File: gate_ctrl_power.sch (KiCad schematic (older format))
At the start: 1 part

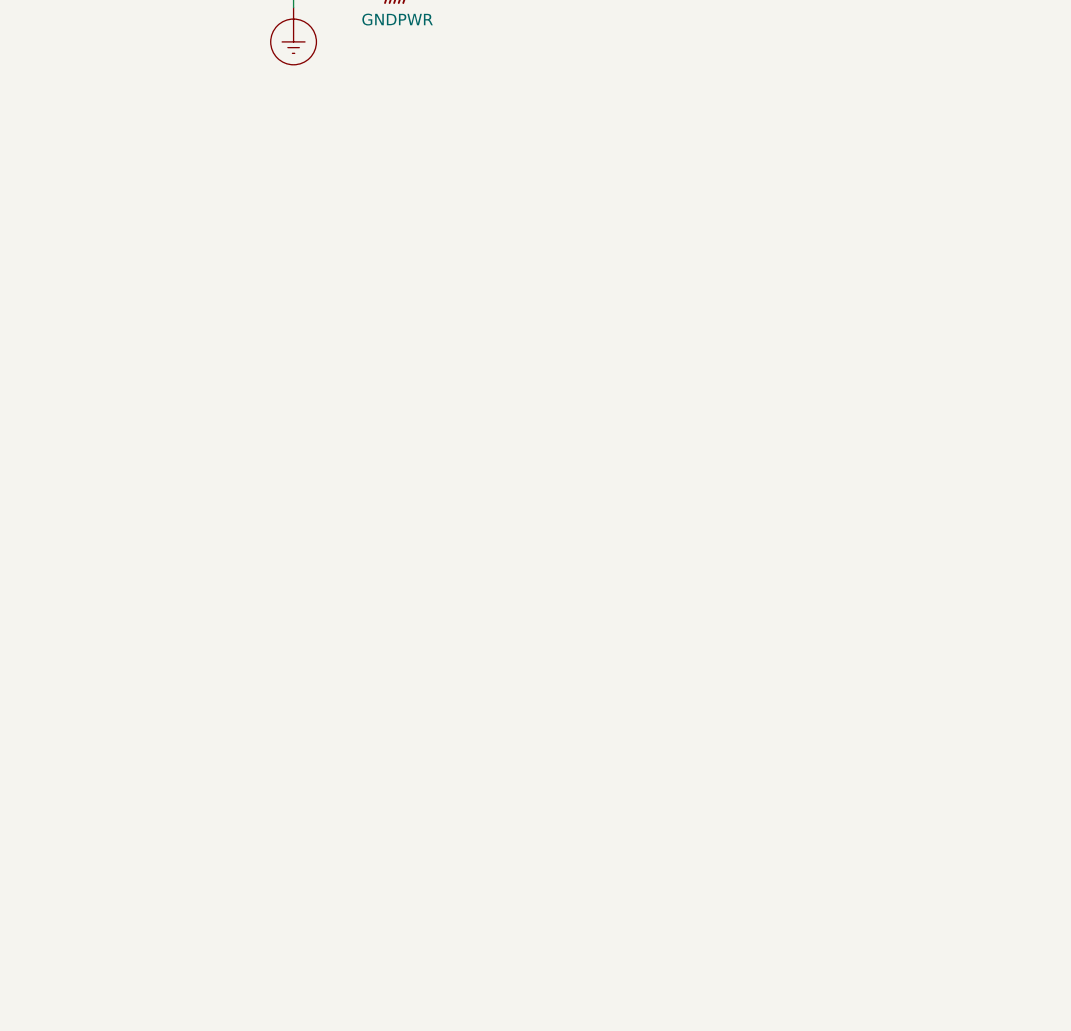
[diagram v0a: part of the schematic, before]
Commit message: Added outputs page, leds.
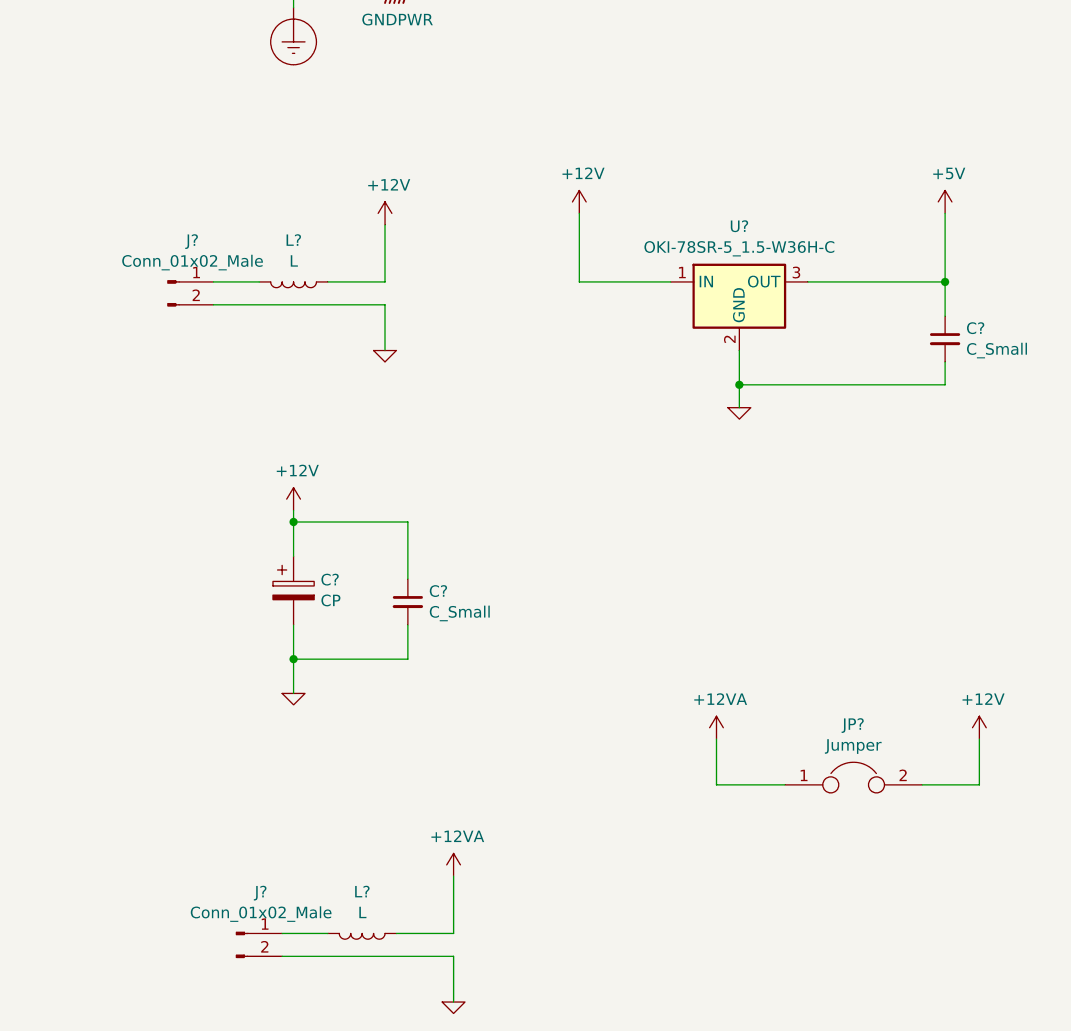
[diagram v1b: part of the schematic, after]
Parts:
- added C? (x2): C_Small, symbol Device:C_Small
- added C?: CP, symbol Device:CP
- added J? (x2): Conn_01x02_Male, symbol Connector:Conn_01x02_Male
- added JP?: Jumper, symbol Device:Jumper
- added L? (x2): L, symbol Device:L
- added U?: OKI-78SR-5_1.5-W36H-C, Converter_DCDC:Converter_DCDC_muRata_OKI-78SR_Horizontal, symbol Converter_DCDC:OKI-78SR-5_1.5-W36H-C
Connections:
- new net: J?.1 (Pin_1), L?.2 (x2)
- new net +12V: C?.1, C?.1, JP?.2, L?.1, U?.1 (IN)
- new net +12VA: JP?.1, L?.1
- new net +5V: C?.1, U?.3 (OUT)
- new net GND: C?.2, C?.2, C?.2, J?.2 (Pin_2), J?.2 (Pin_2), U?.2 (GND)

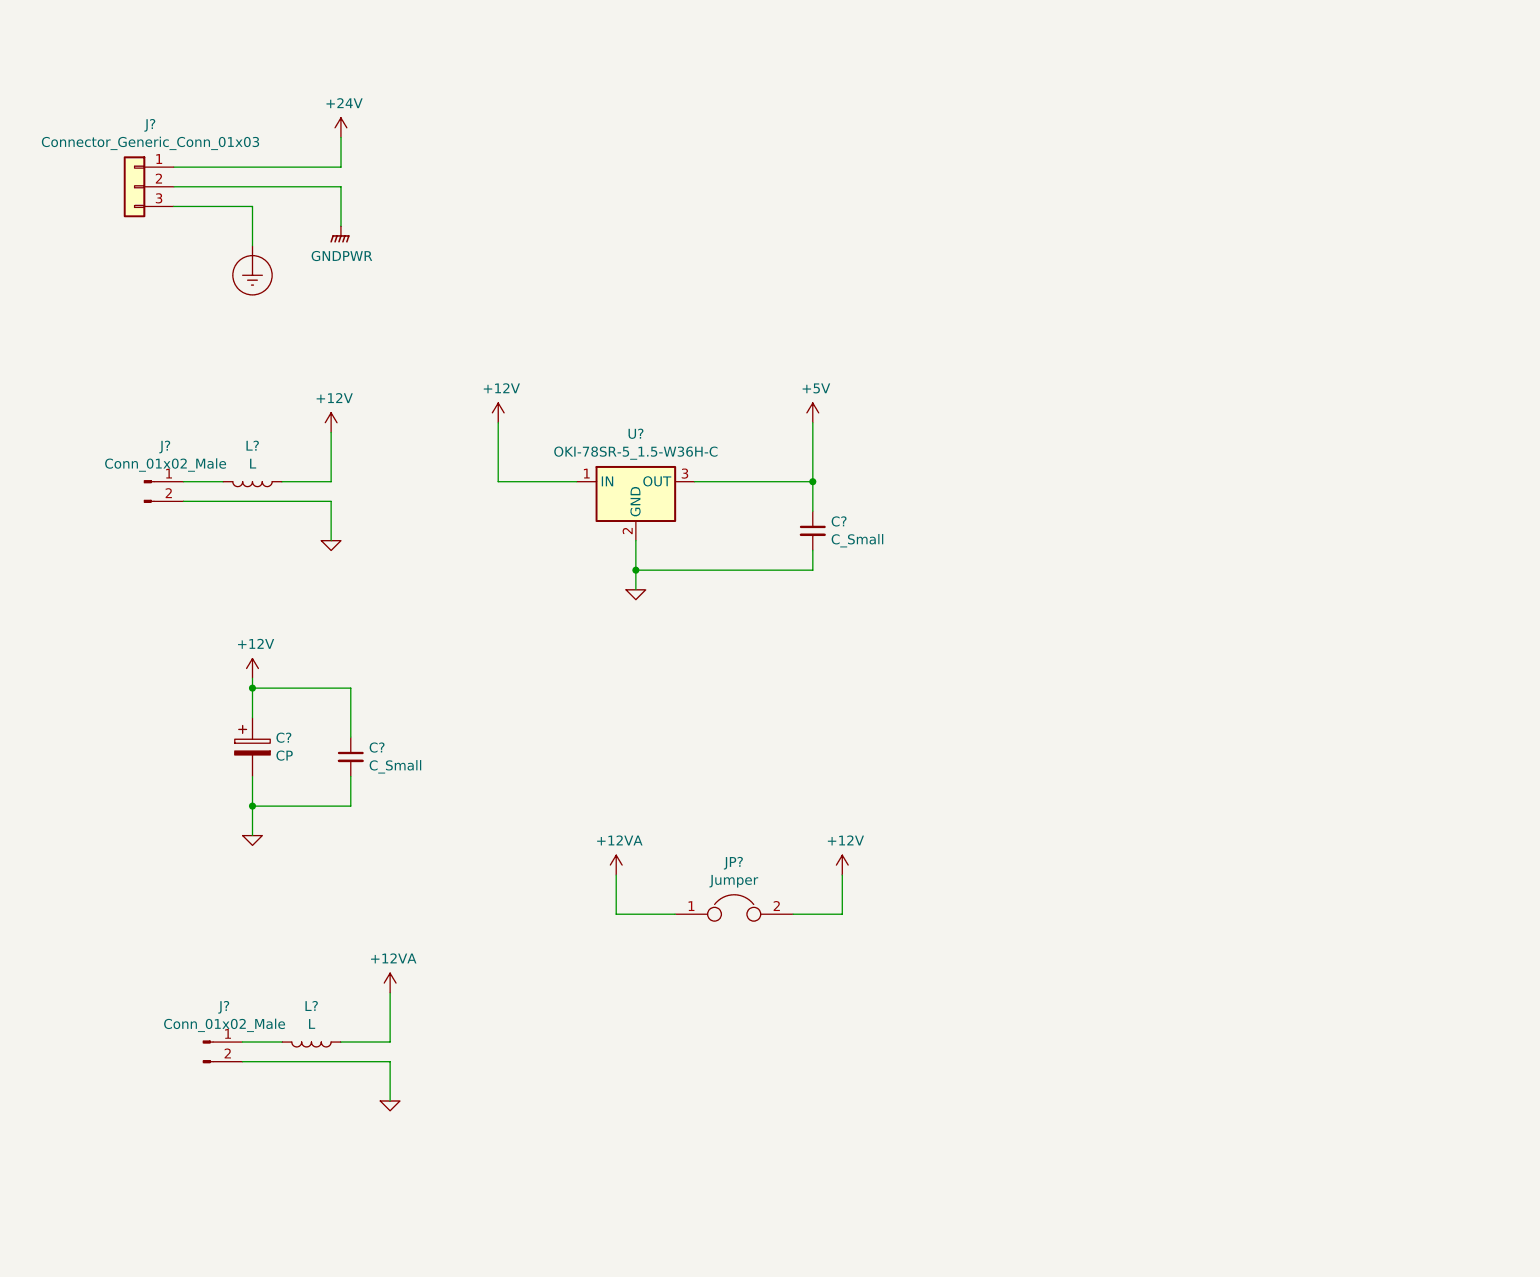
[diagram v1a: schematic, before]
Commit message: Added comments and current sense on 24V supply
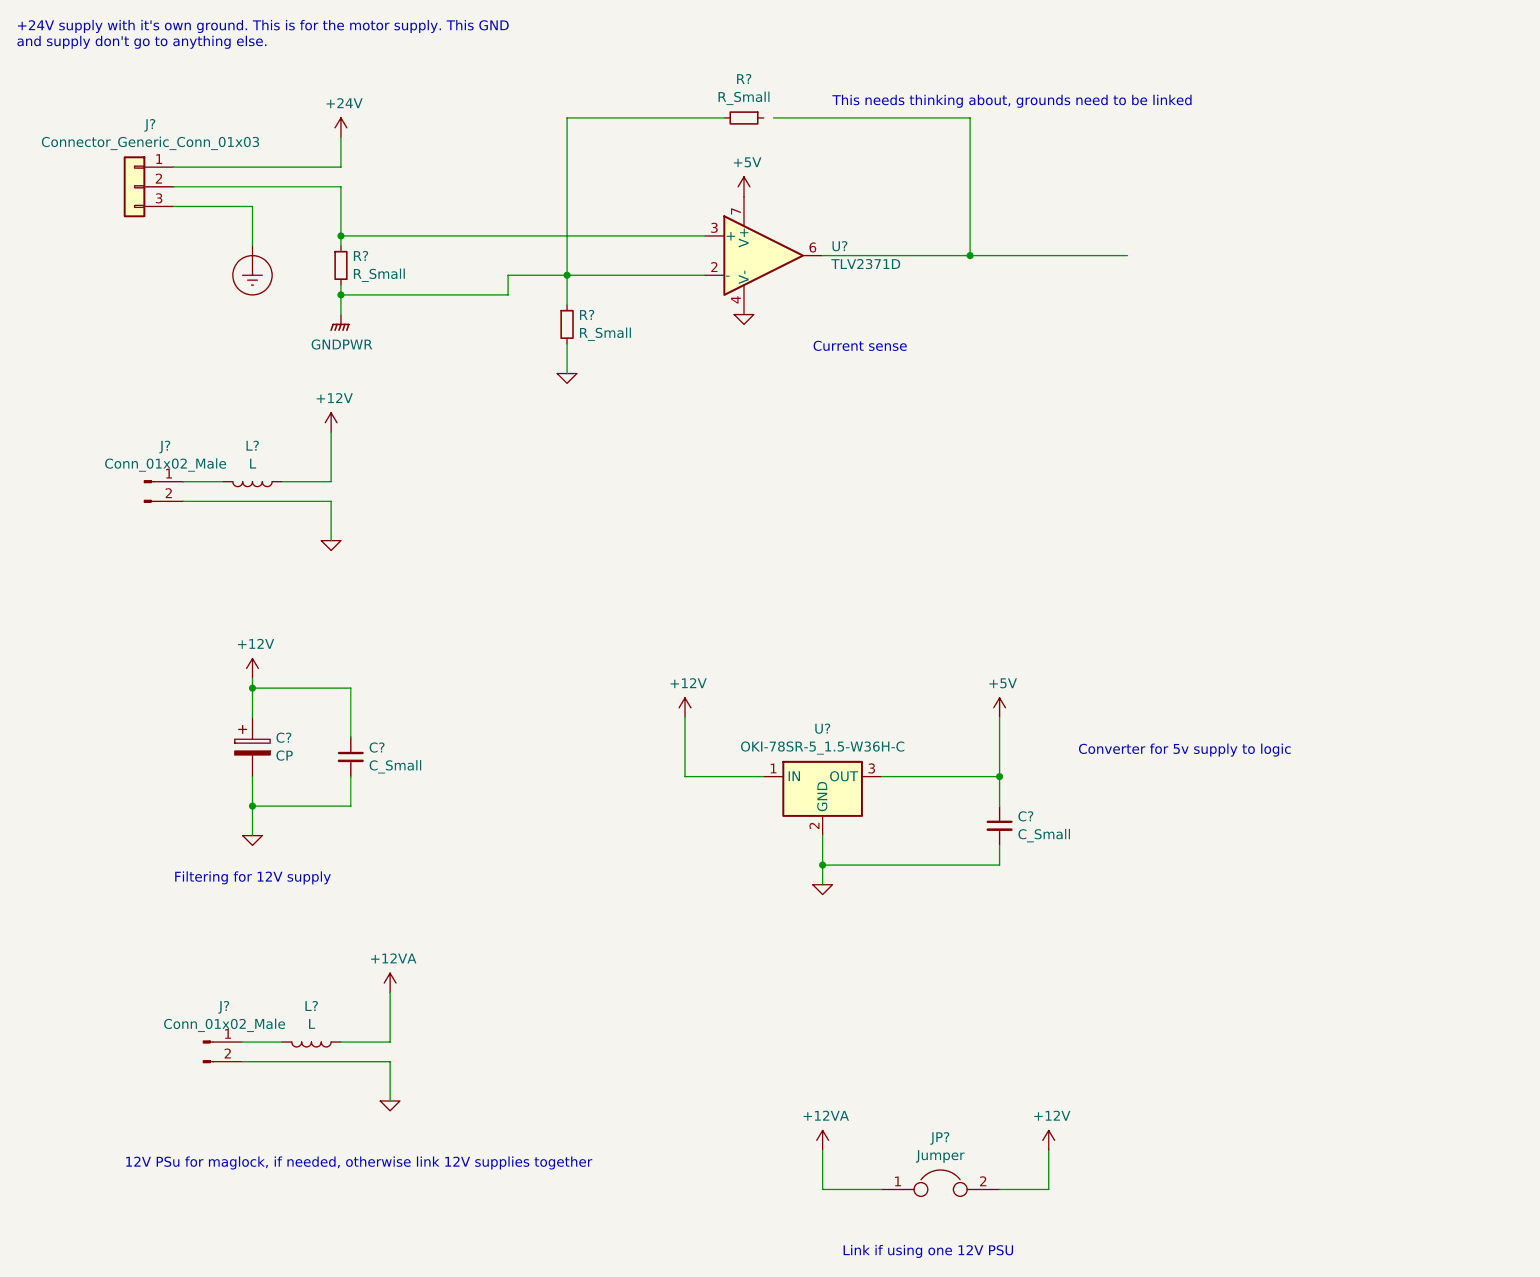
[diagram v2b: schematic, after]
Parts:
- added R? (x3): R_Small, symbol Device:R_Small
- added U?: TLV2371D, Package_SO:SOIC-8_3.9x4.9mm_P1.27mm, symbol Amplifier_Operational:TLV2371D
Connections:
- wire segments 37 -> 53
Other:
- note added: "+24V supply with it's own ground. This is for the motor supply. This GND\nand supply don't go to anything else."
- note added: "12V PSu for maglock, if needed, otherwise link 12V supplies together"
- note added: "Converter for 5v supply to logic"
- note added: "Current sense"
- note added: "Filtering for 12V supply"
- note added: "Link if using one 12V PSU"
- note added: "This needs thinking about, grounds need to be linked"
- moved on the sheet: C?, JP?, U?
